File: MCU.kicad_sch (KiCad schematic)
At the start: 1 part, among them U2 ESP32-C3

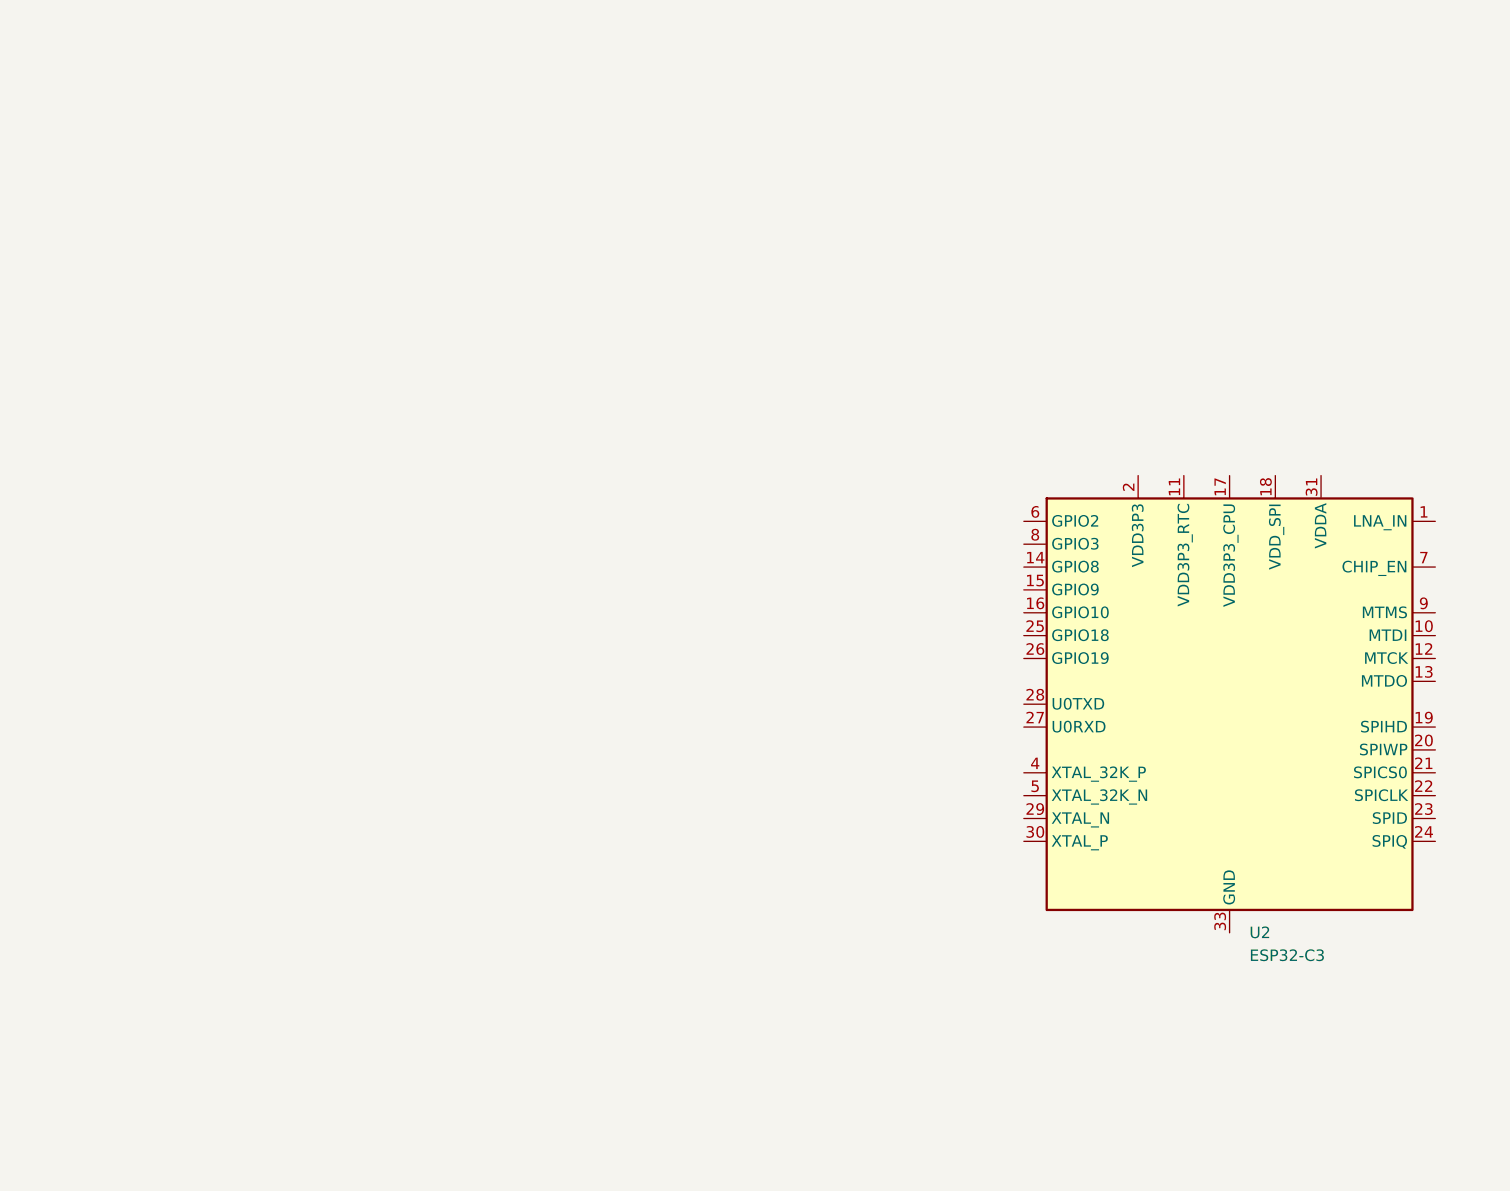
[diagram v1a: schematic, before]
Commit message: route all 3 fets with shunts in a vertical line
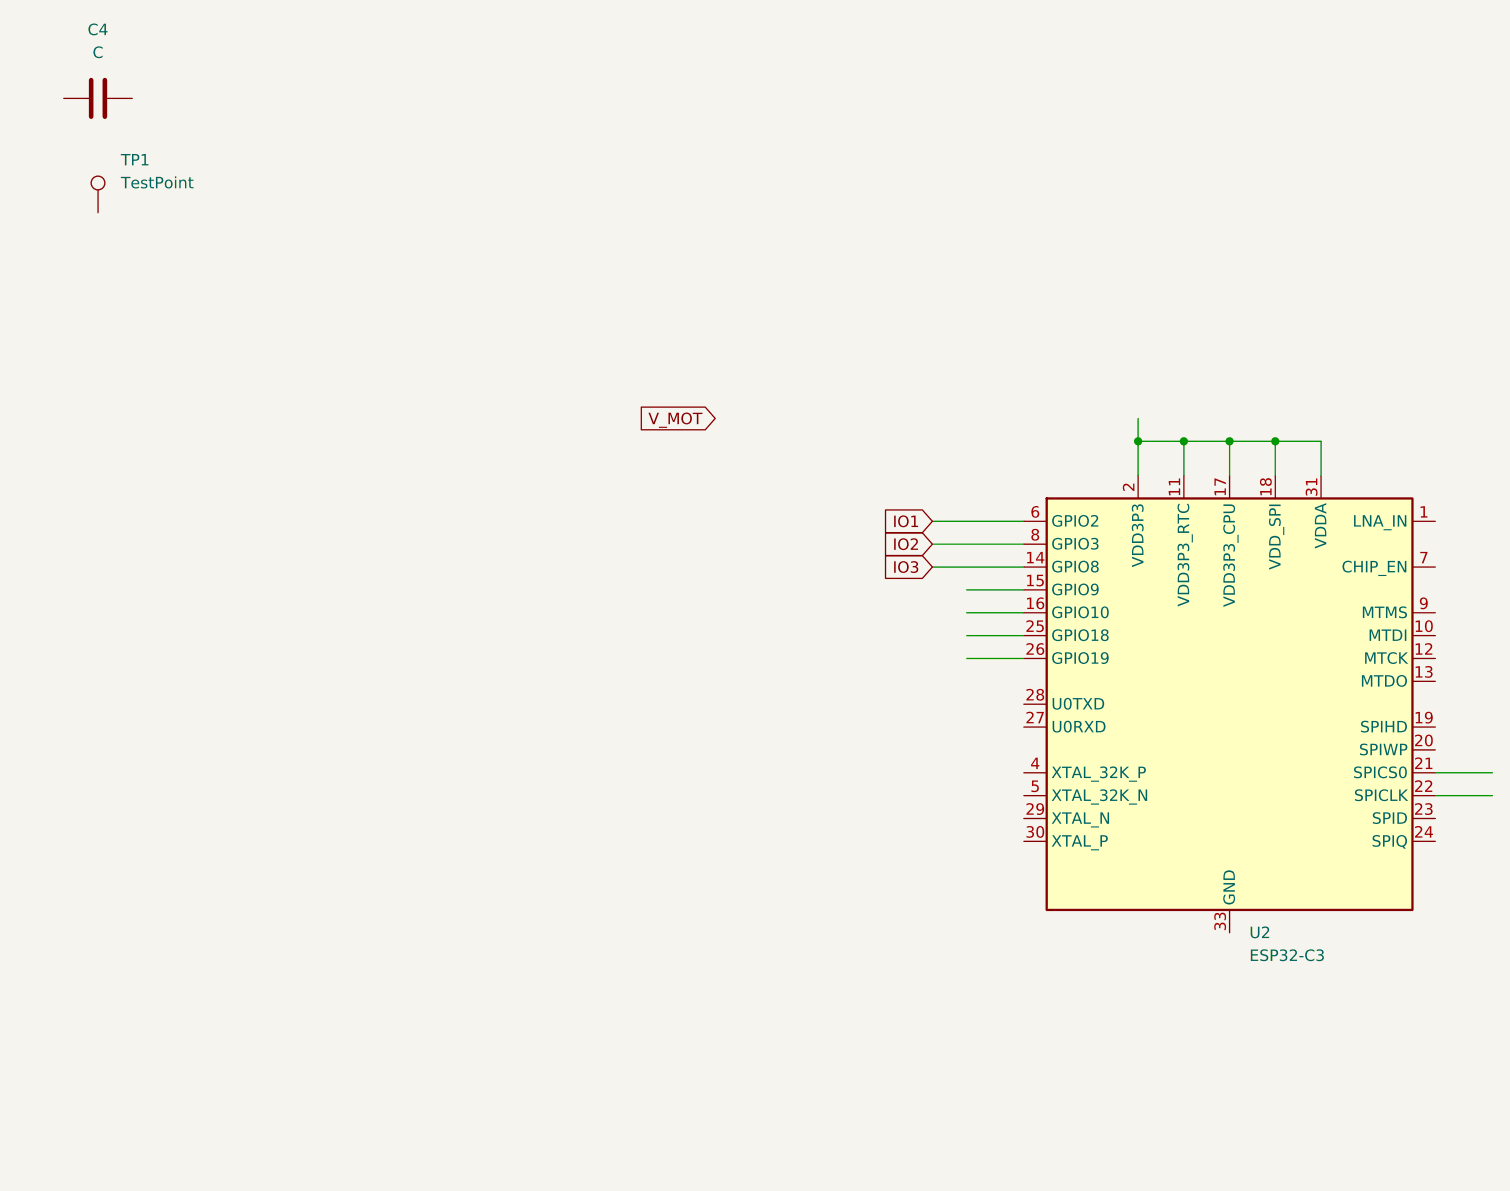
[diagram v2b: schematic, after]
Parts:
- added C4: C, symbol Device:C
- added TP1: TestPoint, TestPoint:TestPoint_Keystone_5019_Miniature, symbol Connector:TestPoint
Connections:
- net at U2.11 (VDD3P3_RTC): now also U2.17 (VDD3P3_CPU), U2.18 (VDD_SPI), U2.2 (VDD3P3), U2.3 (VDD3P3), U2.31 (VDDA), U2.32 (VDDA)
- net IO3: now reaches U2.14 (GPIO8)
- net IO1: now reaches U2.6 (GPIO2)
- net IO2: now reaches U2.8 (GPIO3)

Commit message: using vias on SNA/SPA instead of GxA b/c switching speed
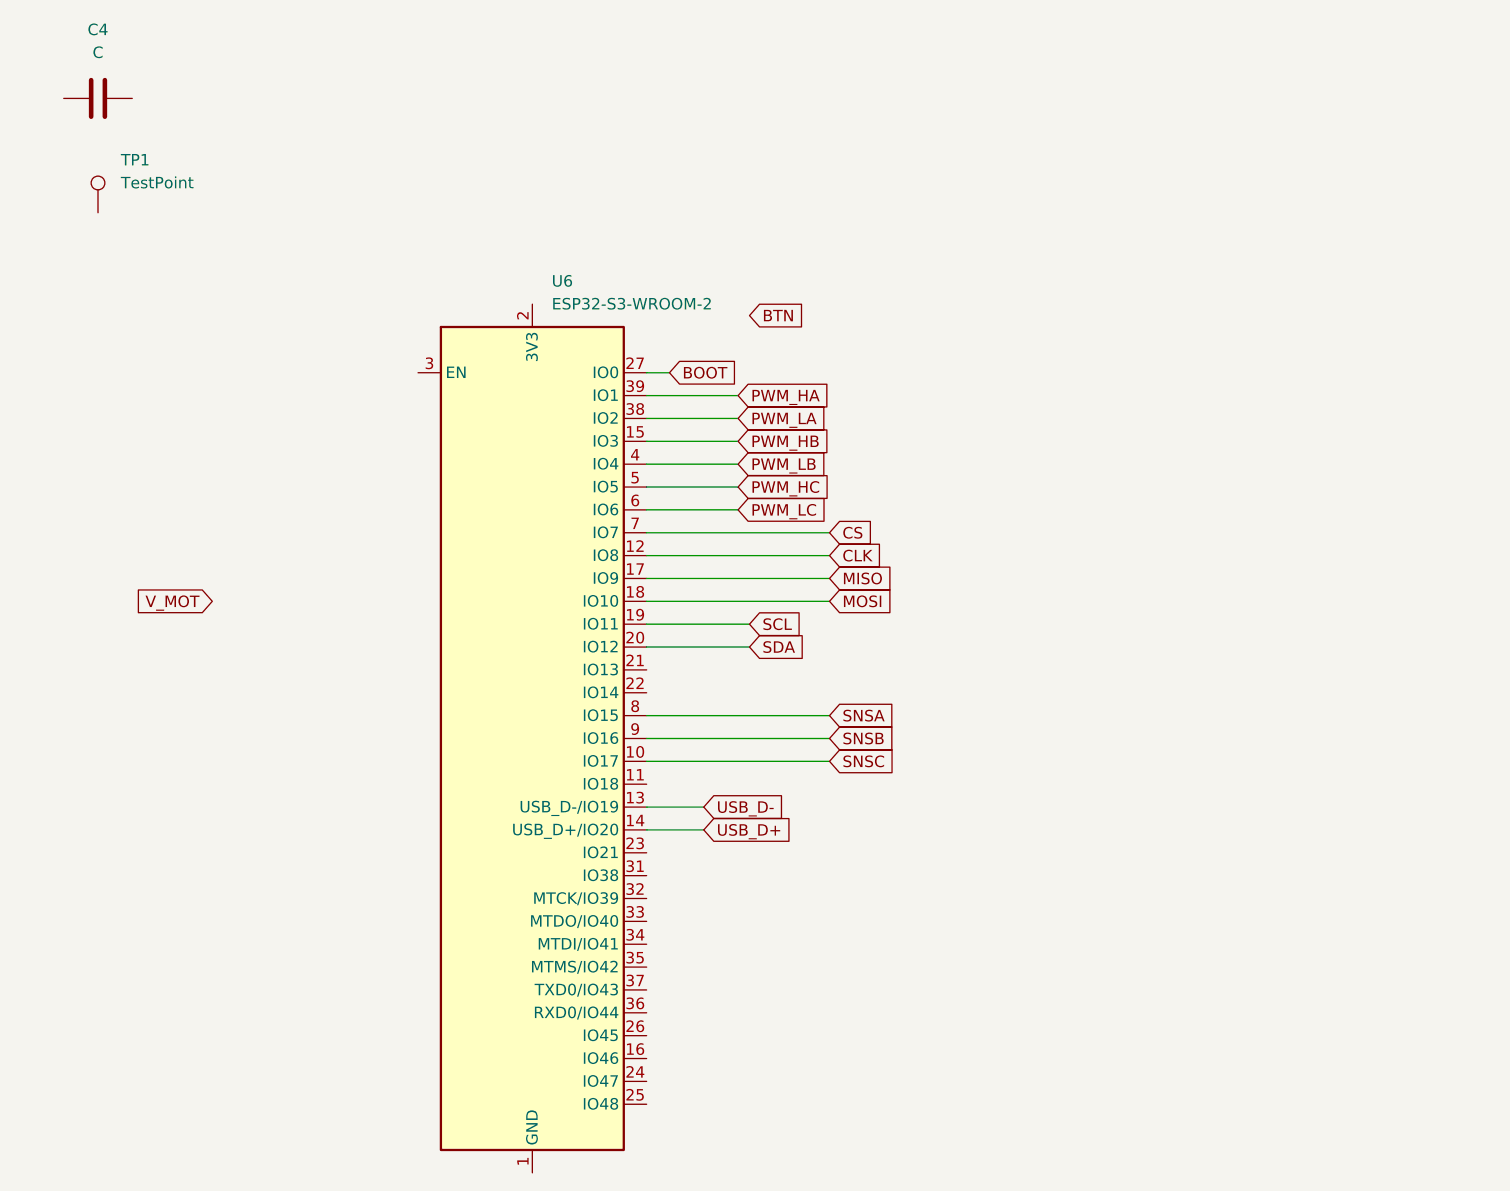
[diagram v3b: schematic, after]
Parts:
- removed U2: ESP32-C3, Package_DFN_QFN:QFN-32-1EP_5x5mm_P0.5mm_EP3.7x3.7mm, symbol MCU_Espressif:ESP32-C3
- added U6: ESP32-S3-WROOM-2, RF_Module:ESP32-S3-WROOM-2, symbol RF_Module:ESP32-S3-WROOM-2
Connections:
- new net: U6.1 (GND), U6.40 (GND), U6.41 (GND)
- new net BOOT: U6.27 (IO0)
- new net CLK: U6.12 (IO8)
- new net CS: U6.7 (IO7)
- new net MISO: U6.17 (IO9)
- new net MOSI: U6.18 (IO10)
- new net PWM_HA: U6.39 (IO1)
- new net PWM_HB: U6.15 (IO3)
- new net PWM_HC: U6.5 (IO5)
- new net PWM_LA: U6.38 (IO2)
- new net PWM_LB: U6.4 (IO4)
- new net PWM_LC: U6.6 (IO6)
- new net SCL: U6.19 (IO11)
- new net SDA: U6.20 (IO12)
- new net SNSA: U6.8 (IO15)
- new net SNSB: U6.9 (IO16)
- new net SNSC: U6.10 (IO17)
- new net USB_D+: U6.14 (USB_D+/IO20)
- new net USB_D-: U6.13 (USB_D-/IO19)

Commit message: selected mcu pins for sense in, SPI
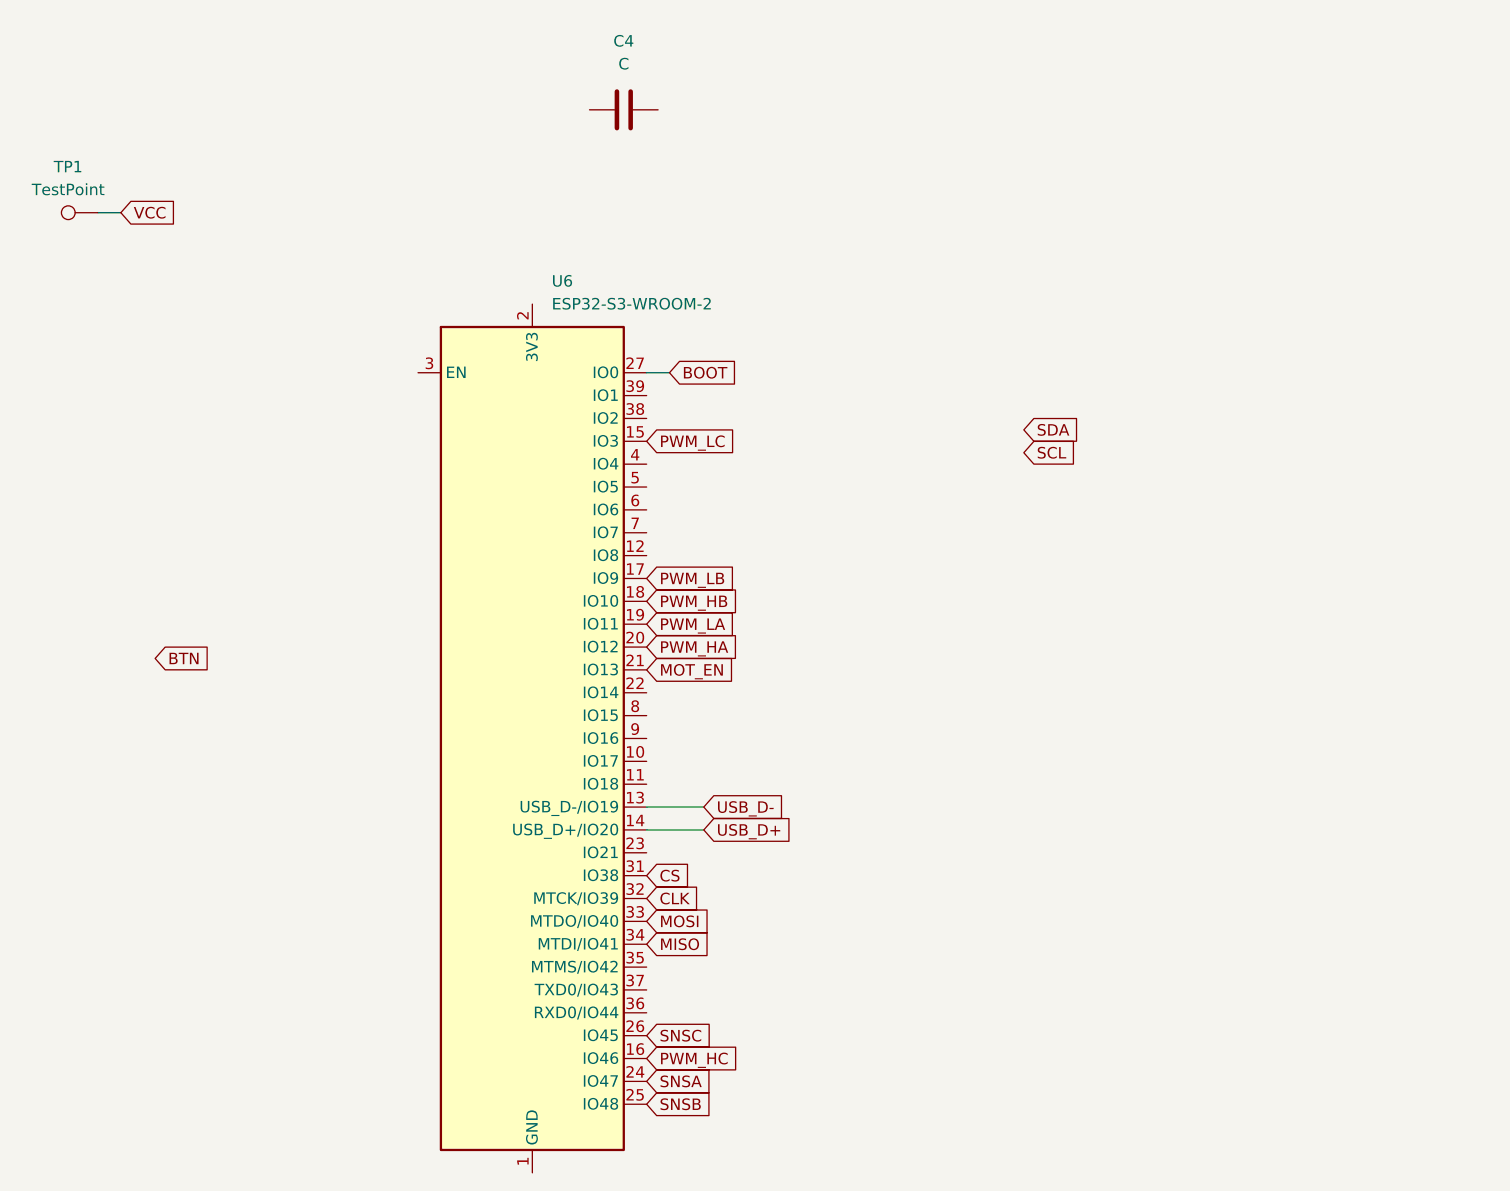
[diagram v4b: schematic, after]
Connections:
- net CLK: now also U6.32 (MTCK/IO39); no longer U6.12 (IO8)
- net CS: now also U6.31 (IO38); no longer U6.7 (IO7)
- net MISO: now also U6.34 (MTDI/IO41); no longer U6.17 (IO9)
- net MOSI: now also U6.33 (MTDO/IO40); no longer U6.18 (IO10)
- net PWM_HA: now also U6.20 (IO12); no longer U6.39 (IO1)
- net PWM_HB: now also U6.18 (IO10); no longer U6.15 (IO3)
- net PWM_HC: now also U6.16 (IO46); no longer U6.5 (IO5)
- net PWM_LA: now also U6.19 (IO11); no longer U6.38 (IO2)
- net PWM_LB: now also U6.17 (IO9); no longer U6.4 (IO4)
- net PWM_LC: now also U6.15 (IO3); no longer U6.6 (IO6)
- net SCL: no longer U6.19 (IO11)
- net SDA: no longer U6.20 (IO12)
- net SNSA: now also U6.24 (IO47); no longer U6.8 (IO15)
- net SNSB: now also U6.25 (IO48); no longer U6.9 (IO16)
- net SNSC: now also U6.26 (IO45); no longer U6.10 (IO17)
- net VCC: now reaches TP1.1
- net MOT_EN: now reaches U6.21 (IO13)
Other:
- moved on the sheet: C4, TP1

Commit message: big layout - lay pgnd and agnd zones and add SPI header pins
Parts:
- removed TP1: TestPoint, TestPoint:TestPoint_Keystone_5019_Miniature, symbol Connector:TestPoint
- C4: footprint (none) -> Capacitor_SMD:C_0805_2012Metric_Pad1.18x1.45mm_HandSolder
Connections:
- net CLK is gone; now on net SNSA: U6.32 (MTCK/IO39)
- net MISO is gone; now on net SNSC: U6.34 (MTDI/IO41)
- net MOSI is gone; now on net SNSB: U6.33 (MTDO/IO40)
- net SNSA: no longer U6.24 (IO47)
- net SNSB: no longer U6.25 (IO48)
- net SNSC: no longer U6.26 (IO45)
- net SPI_CS: now reaches U6.22 (IO14)
- net SPI_CLK: now reaches U6.23 (IO21)
- net CS renamed NFLT
- new net SPI_MISO: U6.25 (IO48)
- new net SPI_MOSI: U6.24 (IO47)
